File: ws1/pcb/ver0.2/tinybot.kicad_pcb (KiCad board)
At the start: 2 copper layers, 50.3 x 49.8 mm, 18 parts, among them IC1 ATTINY84-P, P1 PWR, P2 PIN Breakout, P3 ICSP, P4 M1, P5 M2, U1 LD1117S33TR, U2 L293D

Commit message: updated
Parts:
- P1: footprint Pin_Headers:Pin_Header_Straight_1x02 -> Terminal_Blocks:TerminalBlock_Pheonix_MPT-2.54mm_2pol
- moved U1 20.8 mm to (133.6, 98.8), turned to 90 degrees
- moved IC1 18.3 mm to (142.7, 76.2), turned to 180 degrees
- moved JP2 11.1 mm to (143.3, 97.5)
- moved U2 10.4 mm to (143.0, 88.9), turned to 0 degrees
- moved P3 10.4 mm to (149.4, 100.3)
- moved C2 9.60 mm to (140.7, 101.3)
- moved P1 9.18 mm to (142.0, 106.4)
- moved R3 7.73 mm to (133.9, 73.2)
- moved R1 7.38 mm to (151.1, 86.6)
- moved D1 6.65 mm to (151.4, 91.7), turned to 90 degrees
- moved JP1 5.43 mm to (155.2, 93.7)
- moved R2 5.30 mm to (153.7, 72.9)
- moved C1 3.45 mm to (134.4, 92.2), turned to 90 degrees
- moved P4 3.41 mm to (127.5, 84.3), turned to 270 degrees
- moved P5 2.84 mm to (158.8, 86.9), turned to 90 degrees
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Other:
- board size 50.3 x 49.8 mm -> 46.7 x 46.2 mm

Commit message: logo added
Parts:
- added G***: LOGO, tinybot:en-labs, F.SilkS at (171.6, 95.9)

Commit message: added img
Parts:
- moved G*** 30.8 mm to (142.2, 86.4)
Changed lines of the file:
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@@
     (links 53)
     (no_connects 53)
-    (area 119.812999 62.106428 190.086845 111.90188)
+    (area 119.812999 63.932999 166.699001 110.311001)
     (thickness 1.6)
     (drawings 8)
@@
   )
   (module tinybot:en-labs (layer F.SilkS)
-    (at 171.57 95.91)
-    (fp_text reference G*** (at 0 0) (layer F.SilkS) hide
+    (at 142.24 86.36)
+    (fp_text reference G*** (at 2.42 9.5) (layer F.SilkS) hide
       (effects (font (thickness 0.3)))
     )
-    (fp_text value LOGO (at 0.75 0) (layer F.SilkS) hide
+    (fp_text value LOGO (at 1.658 -11.582) (layer F.SilkS) hide
       (effects (font (thickness 0.3)))
     )

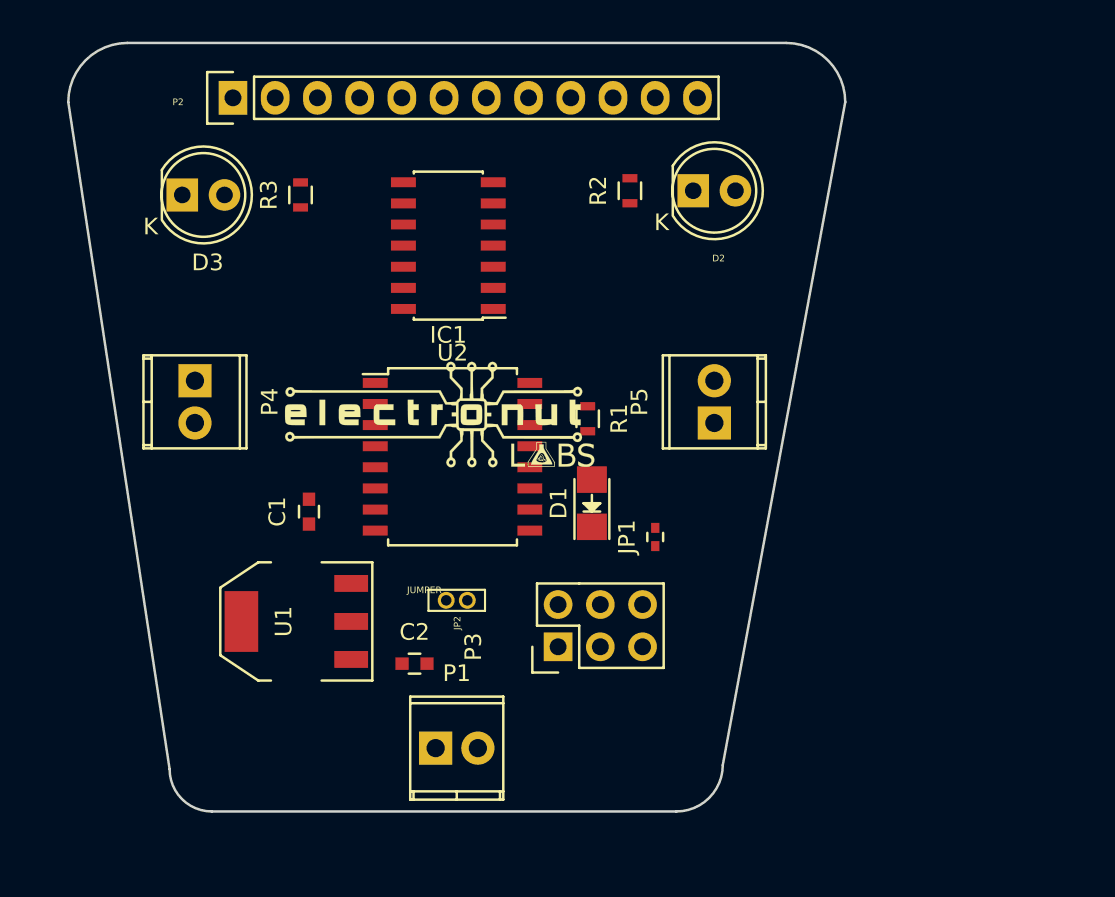
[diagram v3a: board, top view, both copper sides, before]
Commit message: switched to rgb led
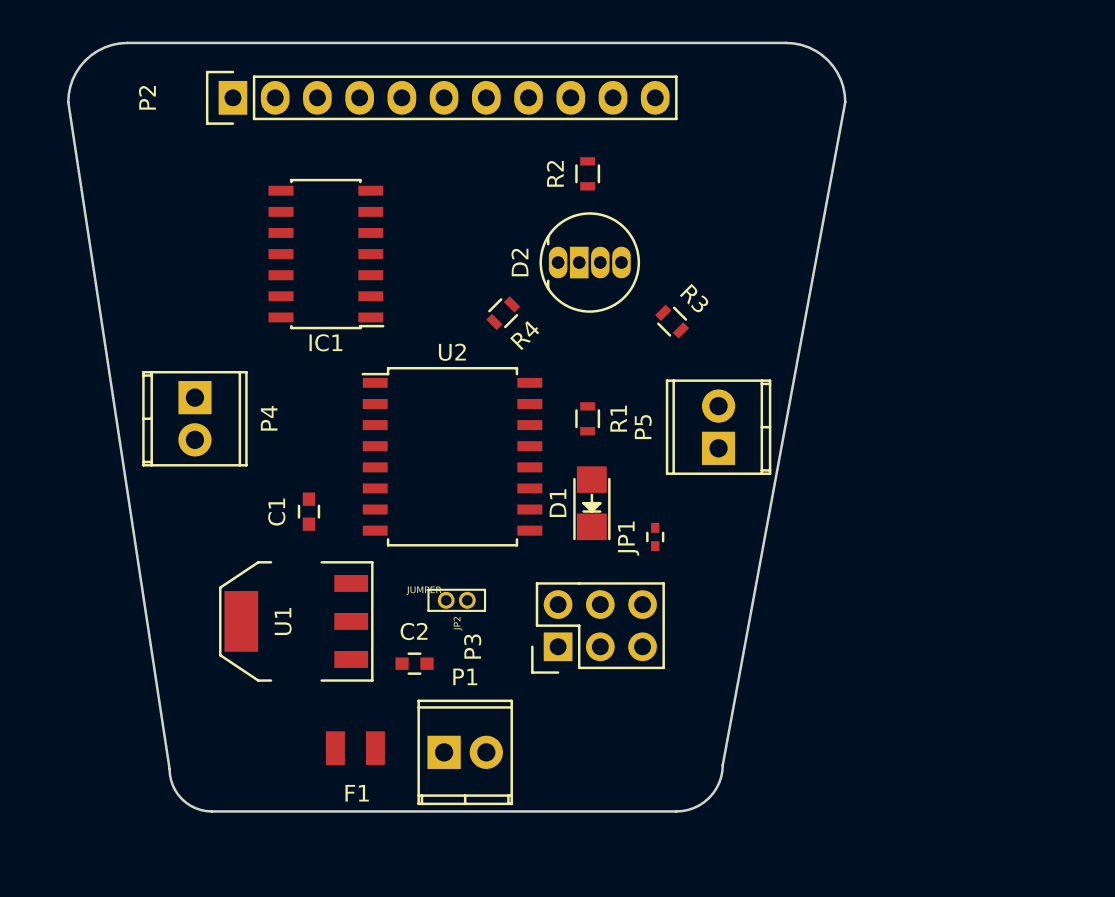
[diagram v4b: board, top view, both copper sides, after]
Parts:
- removed D3: LED, LEDs:LED-5MM
- removed G***: LOGO, tinybot:en-labs
- added F1: FUSE, Fuse_Holders_and_Fuses:Fuse_SMD1206_Reflow, F.Cu at (137.2, 106.4)
- added R4: 100, Resistors_SMD:R_0603, F.Cu at (146.1, 80.3)
- D2: value LED -> LED_RCBG; footprint LEDs:LED-5MM -> LEDs:LED-RGB-5MM_Common_Cathode
- P2: value PIN Breakout -> Pins Breakout; footprint Pin_Headers:Pin_Header_Straight_1x12 -> Pin_Headers:Pin_Header_Straight_1x11
- R2: value 330 -> 200
- R3: value 330 -> 100
- moved R3 23.6 mm to (156.2, 80.8), turned to 315 degrees
- moved D2 9.20 mm to (149.4, 77.2), turned to 90 degrees
- moved IC1 7.38 mm to (135.4, 76.7)
- moved R2 2.74 mm to (151.1, 71.9)
- moved P5 1.55 mm to (159.0, 88.4)
- moved P4 1.02 mm to (127.5, 85.3)
- moved P1 0.57 mm to (142.5, 106.7)
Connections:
- C1 pad 1: VIN -> Net-(C1-Pad1)
- D2 pad 1: GND -> Net-(D2-Pad1)
- D2 pad 2: Net-(D2-Pad2) -> GND
- IC1 pad 11: DIR1B -> Net-(IC1-Pad11)
- IC1 pad 9: SCK -> DIR1B
- P2 pad 1: Net-(IC1-Pad13) -> VCC
- P2 pad 10: DIR2B -> Net-(IC1-Pad5)
- P2 pad 11: Net-(IC1-Pad5) -> RESET
- P2 pad 2: Net-(IC1-Pad12) -> GND
- P2 pad 3: DIR1B -> DIR1A
- P2 pad 4: DIR1A -> DIR1B
- P2 pad 5: SCK -> MISO
- P2 pad 6: MISO -> MOSI
- P2 pad 7: MOSI -> Net-(IC1-Pad6)
- P2 pad 8: Net-(IC1-Pad6) -> DIR2A
- P2 pad 9: DIR2A -> DIR2B
- P3 pad 3: SCK -> DIR1B
- R2 pad 1: Net-(D2-Pad2) -> Net-(D2-Pad3)
- R3 pad 1: Net-(D3-Pad2) -> Net-(D2-Pad4)
- U1 pad 3: VIN -> Net-(C1-Pad1)

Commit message: refining PCB
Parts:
- added JP3: JUMPER, Capacitors_SMD:C_0402, F.Cu at (151.1, 81.5)
- JP2: footprint tinybot:2P-1.27 -> Capacitors_SMD:C_0402
- P2: value Pins Breakout -> Pin Breakout; footprint Pin_Headers:Pin_Header_Straight_1x11 -> tinybot:Pin_Header_Straight_1x14
- moved C1 13.8 mm to (134.0, 106.0)
- moved R1 10.3 mm to (148.3, 96.5)
- moved D1 8.98 mm to (145.0, 98.0), turned to 270 degrees
- moved JP1 8.85 mm to (148.3, 99.3), turned to 270 degrees
- moved P3 5.61 mm to (154.9, 100.8), turned to 180 degrees
- moved P5 5.08 mm to (154.9, 85.3), turned to 260 degrees
- moved P4 4.58 mm to (131.3, 87.9), turned to 98 degrees
- moved P1 2.98 mm to (144.8, 104.8), turned to 180 degrees
- moved P2 2.96 mm to (127.3, 68.8)
- moved JP2 2.41 mm to (141.0, 96.8), turned to 180 degrees
- moved C2 1.55 mm to (141.0, 99.8)
- moved R3 1.02 mm to (156.3, 79.8), turned to 150 degrees
- moved F1 0.74 mm to (137.8, 106.0)
- moved R4 0.63 mm to (146.1, 79.6), turned to 210 degrees
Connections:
- D2 pad 2: GND -> Net-(D2-Pad2)
- P2 pad 10: Net-(IC1-Pad5) -> Net-(IC1-Pad6)
- P2 pad 11: RESET -> DIR2A
- P2 pad 3: DIR1A -> Net-(IC1-Pad13)
- P2 pad 4: DIR1B -> Net-(IC1-Pad12)
- P2 pad 5: MISO -> Net-(IC1-Pad11)
- P2 pad 6: MOSI -> DIR1A
- P2 pad 7: Net-(IC1-Pad6) -> DIR1B
- P2 pad 8: DIR2A -> MISO
- P2 pad 9: DIR2B -> MOSI
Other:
- board size 46.7 x 46.2 mm -> 41.3 x 44.5 mm
- board text added: "5V"
- board text added: "tinyBot 0.2"

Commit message: refining PCB
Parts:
- added G***: LOGO, tinybot:en-labs-fsilk, B.Cu at (143.1, 85.1)
- moved U2 14.6 mm to (150.9, 76.6)
- moved R3 14.1 mm to (147.8, 91.1)
- moved JP3 13.8 mm to (142.5, 92.3)
- moved R4 13.6 mm to (137.5, 90.3)
- moved R2 13.5 mm to (142.5, 82.3)
- moved D2 13.4 mm to (140.8, 87.5)
- moved P2 0.28 mm to (127.1, 69.1)
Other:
- board text added: "GND"
- board text added: "PA0"
- board text added: "PA1"
- board text added: "PA2"
- board text added: "PA3"
- board text added: "PA4"
- board text added: "PA5"
- board text added: "PA6"
- board text added: "PA7"
- board text added: "PB0"
- board text added: "PB1"
- board text added: "PB2"
- board text added: "PB3"

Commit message: refining PCB
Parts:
- removed G***: LOGO, tinybot:en-labs-fsilk
- U2: footprint Housings_SOIC:SOIC-16_7.5x10.3mm_Pitch1.27mm -> Housings_SOIC:SOIC-20_7.5x12.8mm_Pitch1.27mm
- moved P4 2.54 mm to (131.3, 90.4)
- moved P5 2.07 mm to (155.3, 87.4)
- moved U2 1.49 mm to (151.4, 78.0)
